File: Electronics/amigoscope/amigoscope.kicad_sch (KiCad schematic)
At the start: 11 parts, among them J1 USB_C_Receptacle_USB2.0_14P, SW1 RST, SW2 BOOT, U1 ESP32-S3-WROOM-1, U2 NCP1117-3.3_SOT223, U3 TVS1400DRV

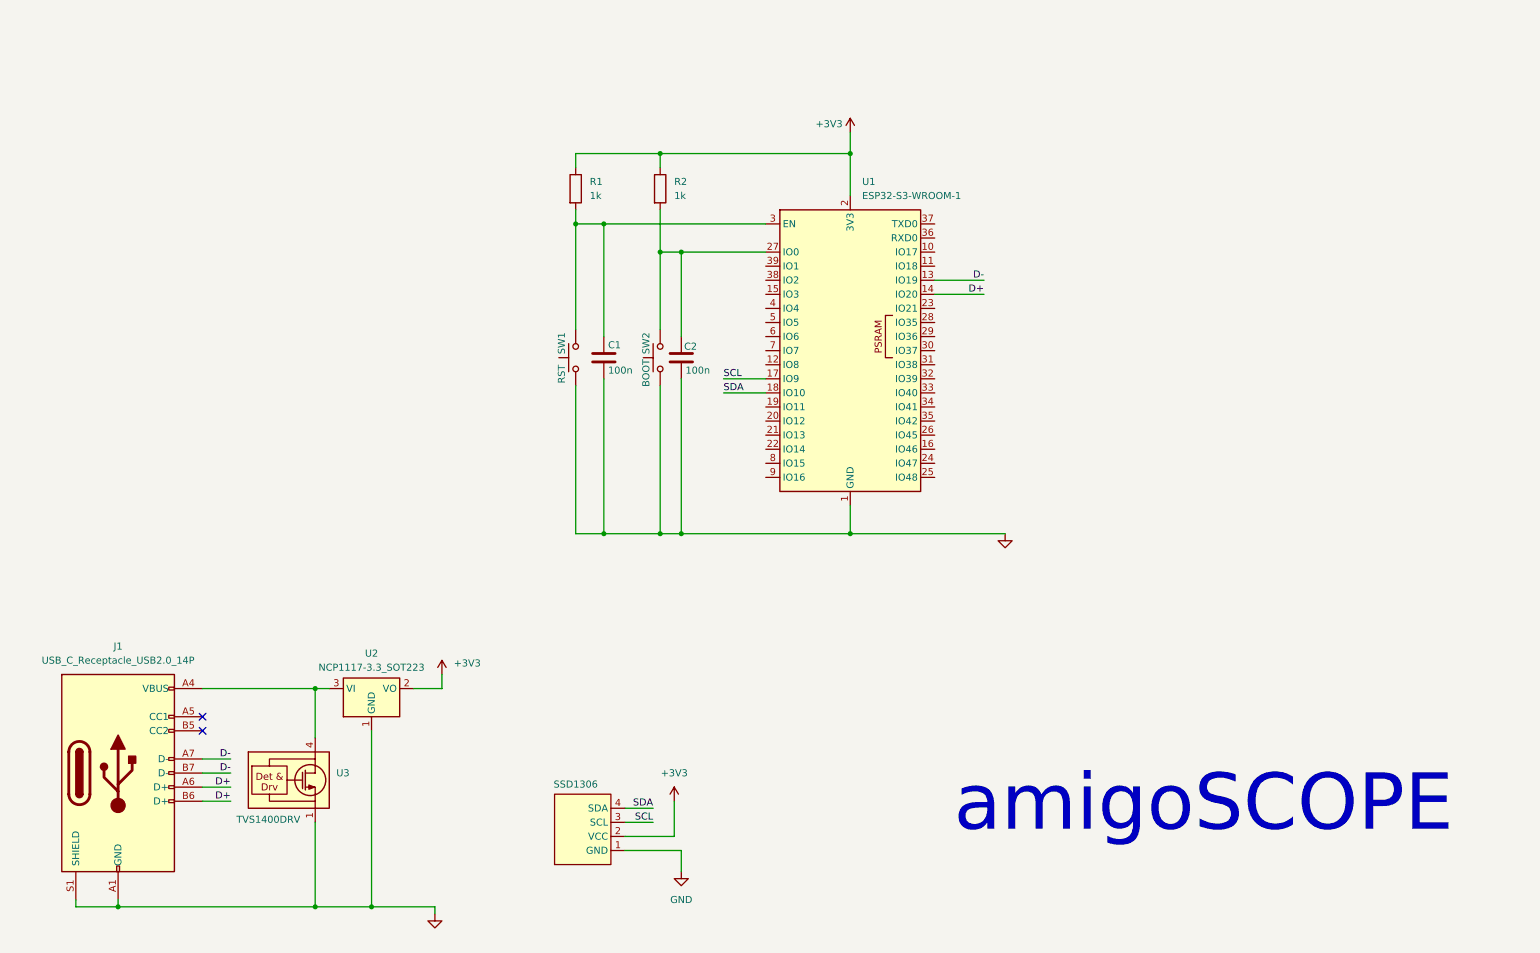
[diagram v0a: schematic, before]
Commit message: finished amigoscope schematic + starting pcb
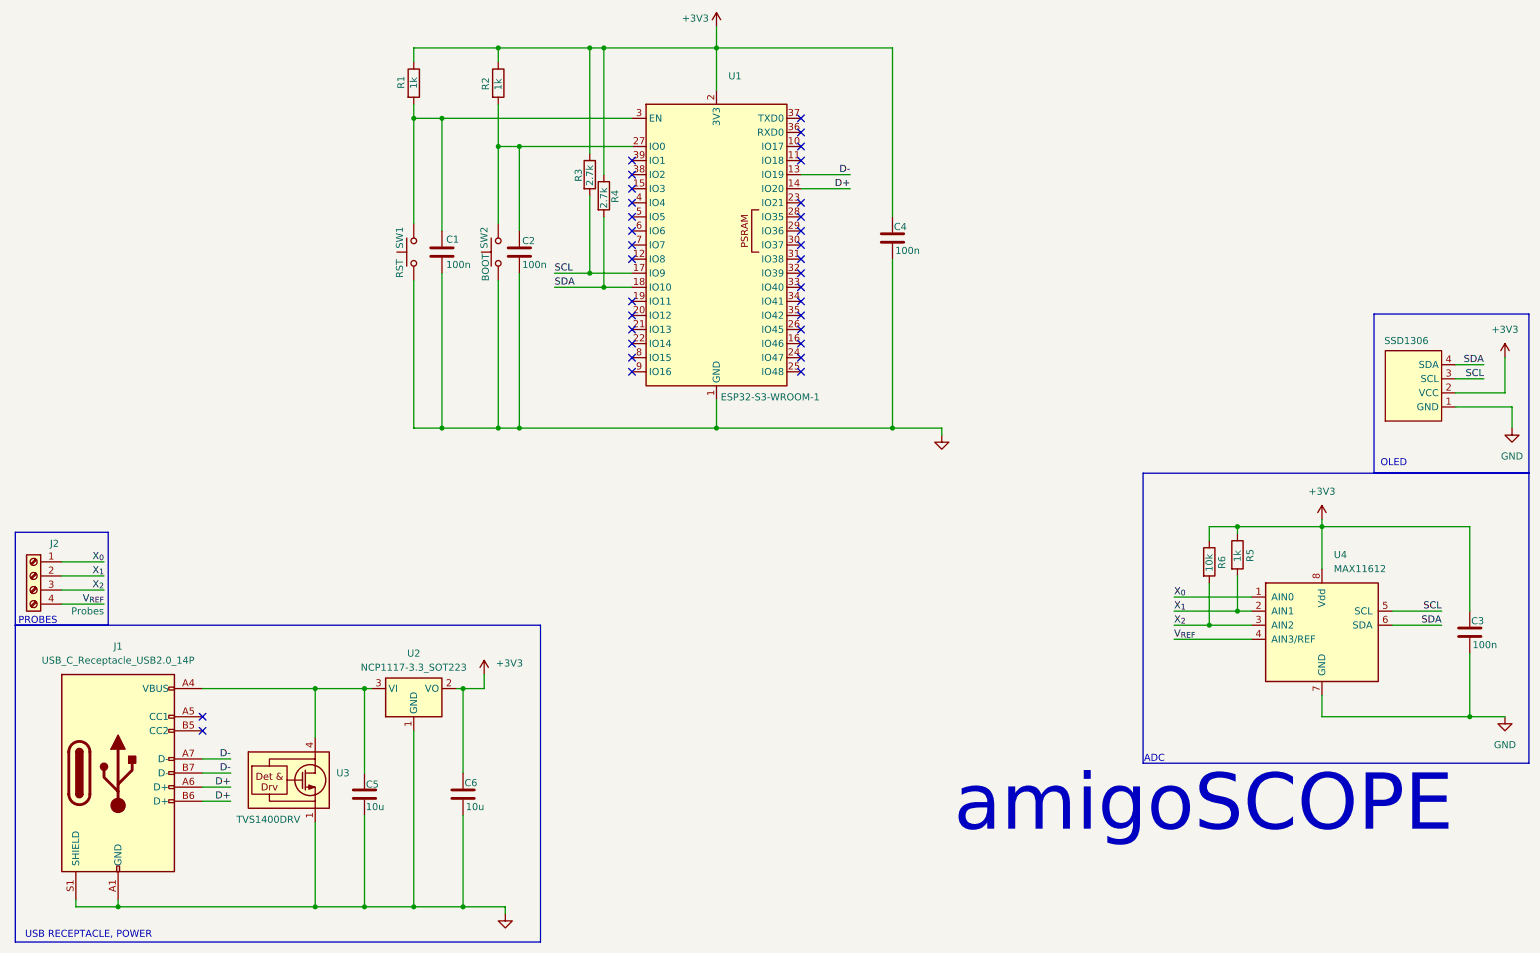
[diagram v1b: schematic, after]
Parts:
- added C3, C4: 100n, Capacitor_SMD:C_0805_2012Metric, symbol Device:C
- added C5, C6: 10u, Capacitor_SMD:C_0805_2012Metric, symbol Device:C
- added J2: Probes, TerminalBlock_Phoenix:TerminalBlock_Phoenix_PT-1,5-4-3.5-H_1x04_P3.50mm_Horizontal, symbol Connector:Screw_Terminal_01x04
- added R3, R4: 2.7k, Resistor_SMD:R_0603_1608Metric, symbol Device:R
- added R5: 1k, Resistor_SMD:R_0603_1608Metric, symbol Device:R
- added R6: 10k, Resistor_SMD:R_0603_1608Metric, symbol Device:R
- added U4: MAX11612, Package_SO:MSOP-8_3x3mm_P0.65mm, symbol Analog_ADC:MAX11612
- C1, C2: footprint (none) -> Capacitor_SMD:C_0805_2012Metric
- J1: footprint (none) -> Connector_USB:USB_C_Receptacle_GCT_USB4105-xx-A_16P_TopMnt_Horizontal
- R1, R2: footprint (none) -> Resistor_SMD:R_0603_1608Metric
- SSD1306: footprint (none) -> Connector_PinSocket_2.54mm:PinSocket_1x04_P2.54mm_Vertical
- SW1, SW2: footprint (none) -> Button_Switch_SMD:SW_Push_1P1T_NO_CK_KMR2
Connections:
- net +3V3: now also C3.1, C4.1, C6.1, R3.1, R4.1, R5.1, R6.1, U4.8 (Vdd)
- net GND: now also C3.2, C4.2, C5.2, C6.2, U4.7 (GND)
- net SCL: now also R3.2, U4.5 (SCL)
- net SDA: now also R4.2, U4.6 (SDA)
- net at J1.A4 (VBUS), J1.A9 (VBUS), J1.B4 (VBUS)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: now also C5.1
- new net V_{REF}: J2.4 (Pin_4), U4.4 (AIN3/REF)
- new net X_{0}: J2.1 (Pin_1), U4.1 (AIN0)
- new net X_{1}: J2.2 (Pin_2), R5.2, U4.2 (AIN1)
- new net X_{2}: J2.3 (Pin_3), R6.2, U4.3 (AIN2)
- no-connect marks 2 -> 33
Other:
- note added: "ADC"
- note added: "OLED"
- note added: "PROBES"
- note added: "USB RECEPTACLE, POWER"
- moved on the sheet: C1, C2, R1, R2, SSD1306, SW1, SW2, U1, U2
